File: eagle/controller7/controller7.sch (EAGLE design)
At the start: 67 parts, among them Q1 MOSFET-NCHANNELBSS138, Q2 MOSFET-NCHANNELBSS138, Q3 MOSFET-NCHANNELBSS138, Q4 MOSFET-NCHANNELBSS138, U1 LM75AIM, U2 MP2307, U3 MP2307, X2 ZX62D-B-5PA8

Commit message: controller6: minor changes
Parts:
- removed H4: MOUNT-HOLE2.8, holes:MOUNT-HOLE2.8
- removed J1: (no value), SparkFun-Connectors:M02LOCK_LONGPADS
- removed J3: (no value), SparkFun-Connectors:M05X2NO_SILK
- removed RTC1: DS3231M, SparkFun-DigitalIC:DS3231M
- removed U1: LM75AIM, NSC_By_element14_Batch_1.1:LM75AIM
- added J4: (no value), SparkFun-Connectors:M02LOCK_LONGPADS
- added J7: (no value), SparkFun-Connectors:M08X2
- added RTC2: DS3231M, SparkFun-DigitalIC:DS3231M
- added U$2: PIZERO_THROUGH_HOLE, pizero:PIZERO_THROUGH_HOLE
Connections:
- removed net N$19: U$1.2, U$1.6
- removed net VBAT: J1.1, RTC1.VBAT
- new net N$12: U$2.2, U$2.6
- new net VBAT1: J4.1, RTC2.VBAT
- net CONV_5V: no longer J3.1
- net GND: now also J4.2, RTC2.GND; no longer J1.2, J3.5, RTC1.GND, U1.GND
- net N$13: no longer J3.8
- net RX: no longer J3.7
- net SCL: now also RTC2.SCL; no longer RTC1.SCL, U1.SCL
- net SDA: now also RTC2.SDA; no longer RTC1.SDA, U1.SDA
- net TX: no longer J3.9
- net VCC: now also RTC2.VCC; no longer RTC1.VCC, U1.+VS
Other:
- moved on the sheet: JP2, VD5, VD6

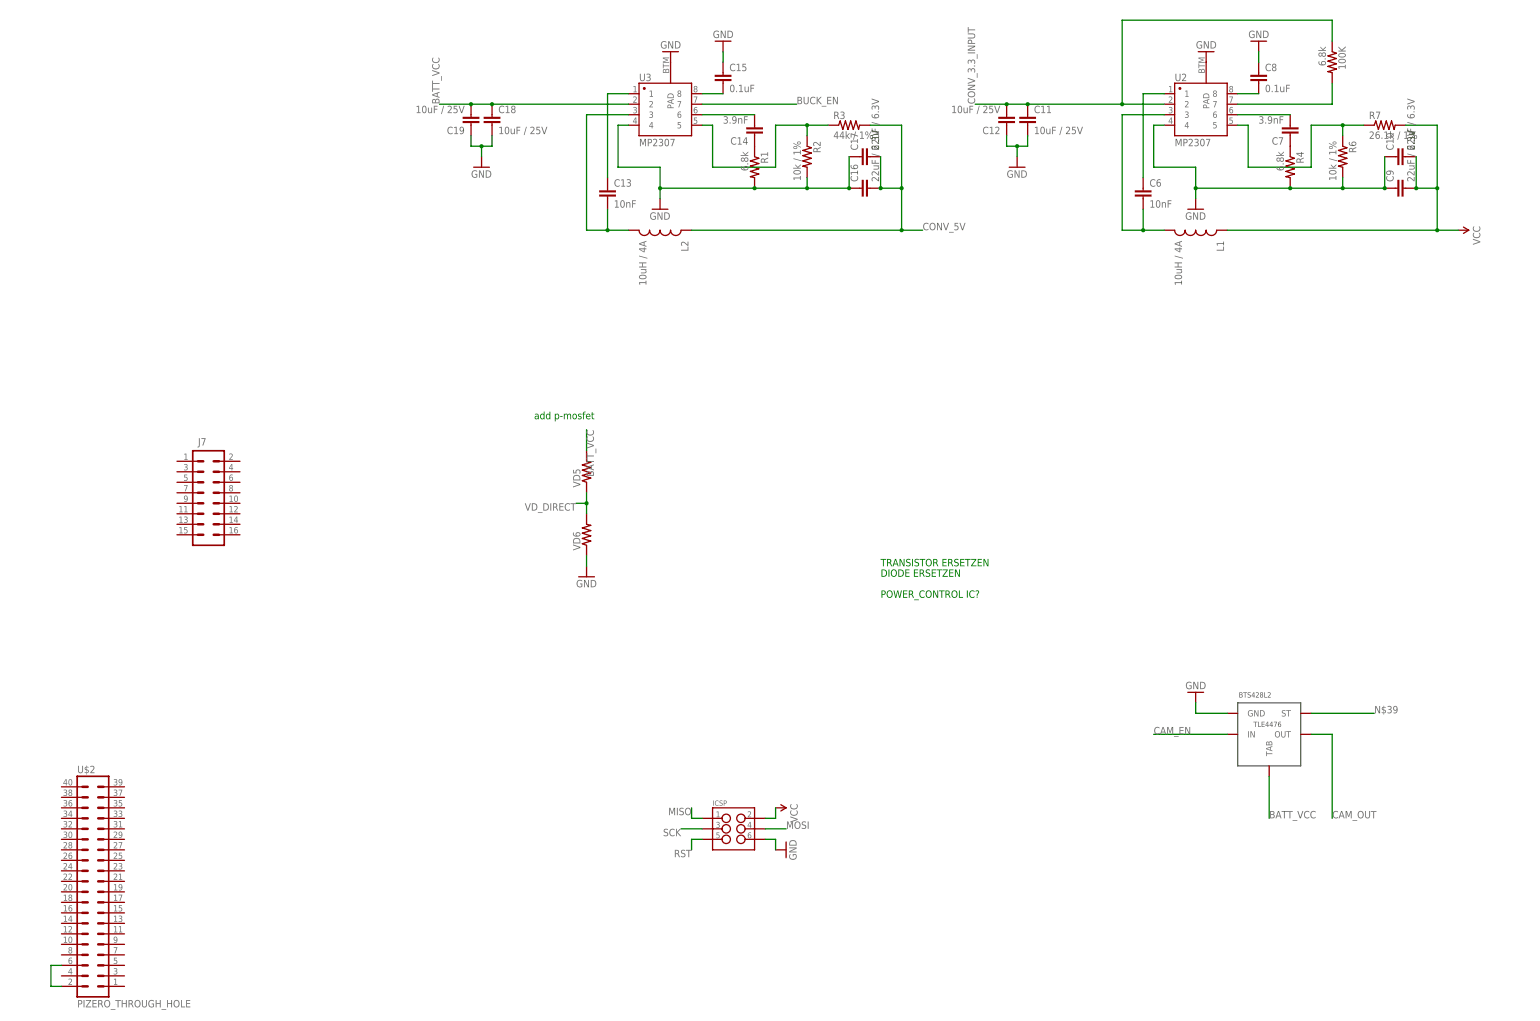
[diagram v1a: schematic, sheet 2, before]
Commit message: controller7: profet added
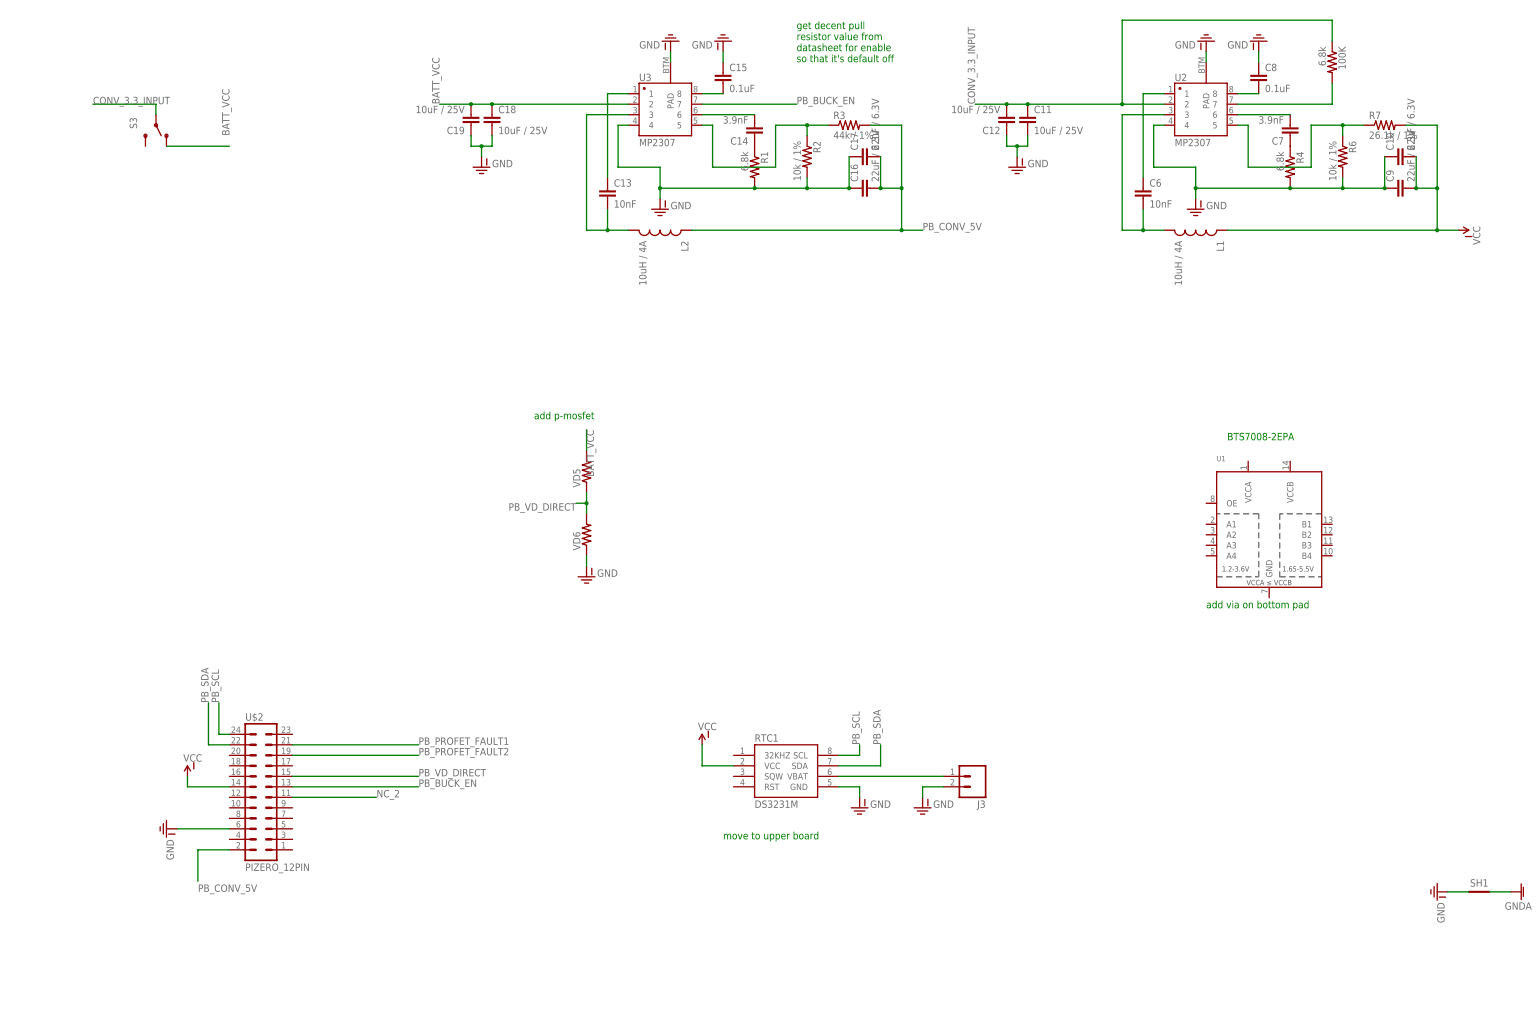
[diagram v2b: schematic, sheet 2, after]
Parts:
- removed BTS428L2: VOLTAGE_REGULATOR_TLE4476, to252:VOLTAGE_REGULATOR_TLE4476
- removed ICSP: (no value), SparkFun-Connectors:M03X2FEMALE
- removed J7: (no value), SparkFun-Connectors:M08X2
- removed JP2: JUMPER-PAD-2-NOYES_SILK, SparkFun-Passives:JUMPER-PAD-2-NOYES_SILK
- removed RTC2: DS3231M, SparkFun-DigitalIC:DS3231M
- removed S2: (no value), SparkFun-Electromechanical:SWITCH-SPDTPTH_LOCK
- removed SH: SHORT-HT5, shorts-old:SHORT-HT5
- added ICSP1: (no value), SparkFun-Connectors:M03X2FEMALE
- added J1: (no value), SparkFun-Connectors:M02LOCK
- added J3: (no value), SparkFun-Connectors:M02LOCK_LONGPADS
- added RTC1: DS3231M, SparkFun-DigitalIC:DS3231M
- added S3: (no value), SparkFun-Electromechanical:SWITCH-SPDTPTH_LOCK
- added SH1: SHORT-HT5, shorts-old:SHORT-HT5
- added U1: (no value), SparkFun-DigitalIC:TXB0104PWRSOIC14
- J4: device SparkFun-Connectors:M02LOCK_LONGPADS -> SparkFun-Connectors:M05X2PTH
- U$1, U$2: value PIZERO_THROUGH_HOLE -> PIZERO_12PIN; device pizero:PIZERO_THROUGH_HOLE -> pizero:PIZERO_12PIN
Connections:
- removed net CAM_EN: BTS428L2.IN, U$3.PC6(OC3A/!OC4A)
- removed net FOO1: U$3.PB5(OC1A/ADC12/!OC4B)
- removed net N$13: JP2.1
- removed net N$39: BTS428L2.ST
- removed net VBAT1: J4.1, RTC2.VBAT
- new net CAM_EN1: U$1.20, U$3.PB6(OC1B/OC4B/ADC13)
- new net CAM_EN2: U$1.18, U$3.PB5(OC1A/ADC12/!OC4B)
- new net CAM_OUT2: J1.2
- new net FOO: U$3.PC6(OC3A/!OC4A)
- new net GND-ISO: C10.1, C11.2, C12.1, C15.1, C16.1, C17.1, C18.2, C19.1, C8.1, C9.1, J3.2, R1.2, R2.2, R4.2, R6.2, RTC1.GND, SH1.P$1, U$2.6, U2.4, U2.PAD, U3.4, U3.PAD, VD6.1
- new net NC: U$1.11
- new net NC_2: U$2.11
- new net PB_BUCK_EN: U$2.13, U3.7
- new net PB_CONV_5V: C16.2, C17.2, L2.1, R3.2, U$2.2
- new net PB_PROFET_FAULT1: U$2.21
- new net PB_PROFET_FAULT2: U$2.19
- new net PB_SCL: RTC1.SCL, U$2.24
- new net PB_SDA: RTC1.SDA, U$2.22
- new net PB_VD_DIRECT: U$2.15, VD5.1, VD6.2
- new net PROFET_FAULT1: U$1.21, U$3.PD7(OC4D/ADC10/T0)
- new net PROFET_FAULT2: U$1.19, U$3.PD6(T1/ADC9/!OC4D)
- new net VBAT2: J3.1, RTC1.VBAT
- new net VCC-ISO: C10.2, C9.2, L1.1, R7.2, RTC1.VCC
- net BATT_VCC: now also S3.O; no longer BTS428L2.TAB, S2.O
- net BUCK_EN: now also U$1.13; no longer U3.7
- net CAM_OUT: no longer BTS428L2.OUT
- net CONV_3.3_INPUT: now also S3.P; no longer S2.P
- net CONV_5V: now also U$1.2; no longer C16.2, C17.2, L2.1, R3.2
- net FOO2: now also U$1.17; no longer U$3.PB6(OC1B/OC4B/ADC13)
- net GND: now also ICSP1.6, U$1.6; no longer BTS428L2.GND, C10.1, C11.2, C12.1, C15.1, C16.1, C17.1, C18.2, C19.1, C8.1, C9.1, ICSP.6, R1.2, R2.2, R4.2, R6.2, RTC2.GND, SH.P$1, U2.4, U2.PAD, U3.4, U3.PAD, VD6.1
- net GNDA: now also J1.1, SH1.P$2; no longer SH.P$2
- net MISO: now also ICSP1.1; no longer ICSP.1
- net MOSI: now also ICSP1.4; no longer ICSP.4
- net N$12: now also U$1.16; no longer U$2.2, U$2.6
- net N$22: no longer S2.S
- net RST: now also ICSP1.5; no longer ICSP.5, JP2.2
- net RX: now also U$1.8
- net SCK: now also ICSP1.3; no longer ICSP.3
- net SCL: now also J4.10; no longer RTC2.SCL
- net SDA: now also J4.8; no longer RTC2.SDA
- net TX: now also U$1.10
- net VCC: now also ICSP1.2, J4.4, U$1.14; no longer C10.2, C9.2, ICSP.2, L1.1, R7.2, RTC2.VCC
- net VD_DIRECT: now also U$1.15; no longer VD5.1, VD6.2
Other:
- note added: "BTS7008-2EPA"
- note added: "add via on bottom pad"
- note added: "get decent pull resistor value from datasheet for enable so that it's default off"
- note added: "move to upper board"
- note removed: "3.3V"
- note removed: "5V"
- note removed: "DIODE ERSETZEN"
- note removed: "POWER_CONTROL IC?"
- note removed: "STEP-DOWN-CONVERTER"
- note removed: "Short between Power-GND and Signal-GND"
- note removed: "TRANSISTOR ERSETZEN"
- moved on the sheet: J6, J8, R9

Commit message: controller7: routing power board created display board
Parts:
- removed J6, J8: (no value), SparkFun-Connectors:M02LOCK
- removed Q3, Q4: MOSFET-NCHANNELBSS138, SparkFun-DiscreteSemi:MOSFET-NCHANNELBSS138
- removed RTC1: DS3231M, SparkFun-DigitalIC:DS3231M
- removed U1: (no value), SparkFun-DigitalIC:TXB0104PWRSOIC14
- added IC1, IC2: ILD213T, SparkFun-DiscreteSemi:ILD213T
- added J10, J7, J9: (no value), SparkFun-Connectors:M02LOCK
- added JP1: JUMPER-PAD-2-NOYES_SILK, SparkFun-Passives:JUMPER-PAD-2-NOYES_SILK
- added R15, R18, R19, R20: (no value), SparkFun-Passives:RESISTOR0805-RES
- added R16, R17, R21, R22, R30: (no value), SparkFun-Passives:RESISTOR1206
- added RTC2: DS3231M, SparkFun-DigitalIC:DS3231M
- added RV1: (no value), SparkFun-Electromechanical:POT
- added S2, S4, S5, S6: (no value), SparkFun-Retired:TAC_SWITCHPTH
- added U$7: BTS7008-2EPA, SparkFun-DigitalIC:BTS7008-2EPA
- added U$8: PIZERO_12PIN, pizero:PIZERO_12PIN
- added X1: 1501_04, con-lumberg:1501_04
- C3: device SparkFun-Passives:CAP0805 -> SparkFun-Passives:CAP1206
- J1: device SparkFun-Connectors:M02LOCK -> SparkFun-Connectors:M04LOCK
- J3: device SparkFun-Connectors:M02LOCK_LONGPADS -> SparkFun-Connectors:M04LOCK
- J4: device SparkFun-Connectors:M05X2PTH -> SparkFun-Connectors:M02PTH
- L1, L2: device SparkFun-Passives:INDUCTORSDR0403-560KL -> SparkFun-Passives:INDUCTORSRU1038
- Q1: value MOSFET-NCHANNELBSS138 -> 2.5A/30V; device SparkFun-DiscreteSemi:MOSFET-NCHANNELBSS138 -> SparkFun-DiscreteSemi:MOSFET-PCHANNELDMG2307L
- Q2: value MOSFET-NCHANNELBSS138 -> 200mA/50V
- R11, R12, R13, R14, RUSB1, RUSB2: device SparkFun-Passives:RESISTOR0805-RES -> SparkFun-Passives:RESISTOR1206
- U$2: value PIZERO_12PIN -> PIZERO_10PIN; device pizero:PIZERO_12PIN -> pizero:PIZERO_10PIN
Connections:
- removed net CAM_OUT: J8.2
- removed net CONV_3.3_INPUT: 100K.1, C11.1, C12.2, S3.P, U2.2
- removed net FOO: U$3.PC6(OC3A/!OC4A)
- removed net FOO2: U$1.17
- removed net PB_PROFET_FAULT1: U$2.21
- removed net PB_PROFET_FAULT2: U$2.19
- removed net PB_SCL: RTC1.SCL, U$2.24
- removed net PB_SDA: RTC1.SDA, U$2.22
- removed net PROFET_FAULT1: U$1.21, U$3.PD7(OC4D/ADC10/T0)
- removed net PROFET_FAULT2: U$1.19, U$3.PD6(T1/ADC9/!OC4D)
- removed net VBAT2: J3.1, RTC1.VBAT
- new net 3.3V: J1.2, J3.1, RV1.A, S2.4, S4.4, S5.4, S6.4, U$8.6
- new net ANALOG_IO: U$1.24, U$3.PB6(OC1B/OC4B/ADC13)
- new net BATT_VCC_RAW: J7.2, S3.O
- new net CAM_OUT1: J9.2, U$7.OUT0
- new net DB_ANALOG_IO: RV1.S, U$8.24
- new net DB_BTN: S6.2, U$8.22
- new net DB_SCL: J1.3, J3.3, U$8.21
- new net DB_SDA: J1.4, J3.4, U$8.23
- new net FOO15: U$3.PB7(OC0A/OC1C/RTS)
- new net FOO8: U$3.PB0(SS)
- new net FOOA: U$3.PB4(ADC11)
- new net N$13: IC2.A2, R19.2
- new net N$15: IC1.A2, R15.2
- new net N$19: IC1.A1, R20.2
- new net N$34: IC1.ET1, IC1.ET2, IC2.ET1, IC2.ET2, J2.7, JP1.2, X1.1
- new net N$35: J2.8, Q1.D
- new net N$36: Q1.G, Q2.S, R10.1
- new net N$37: J1.1
- new net N$38: R14.1, S5.2
- new net N$39: R30.2, S4.2
- new net N$40: R21.2, S2.2
- new net N$43: R22.2, RV1.E
- new net PB_CAM_EN1: R11.1, U$2.20, U$7.IN0
- new net PB_CAM_EN2: R12.2, U$2.15, U$7.IN1
- new net PB_PROFET_1: R17.1, U$2.18, U$7.DEN
- new net PB_PROFET_2: U$2.19, U$7.IS
- new net PB_PROFET_3: R16.2, U$2.17, U$7.DSEL
- new net PROFET1: U$1.18, U$3.PF6(ADC6/TDO)
- new net PROFET2: U$1.19, U$3.PF5(ADC5/TMS)
- new net PROFET3: U$1.17, U$3.PF4(ADC4/TCK)
- new net SWITCH_USB_VCC: Q2.G, U$3.PD5(XCK/CTS)
- new net VBAT1: J4.1, RTC2.VBAT
- new net VCC_2: R14.2, R21.1, R22.1, R30.1, U$8.14
- net BATT_VCC: now also 100K.1, C11.1, C12.2, S3.P, U$7.VS, U2.2; no longer J6.2, S3.O
- net BTN: now also U$1.22, U$3.PC7(ICP3/CLK0/OC4A); no longer U$3.PF7(ADC7(TDI)
- net BUCK_EN: now also U$1.16, U$3.PE6(INT.6/AIN0); no longer U$1.13, U$3.PB7(OC0A/OC1C/RTS)
- net CAM1: now also R20.1, U$3.PB5(OC1A/ADC12/!OC4B); no longer Q1.G, R10.2, U$3.PF1(ADC1)
- net CAM2: now also R15.1, U$3.PD7(OC4D/ADC10/T0); no longer Q2.G, R11.2, U$3.PF4(ADC4/TCK)
- net CAM3: now also R18.1, U$3.PD6(T1/ADC9/!OC4D); no longer Q3.G, R12.2, U$3.PF5(ADC5/TMS)
- net CAM4: now also R19.1, U$3.PD4(ICP1/ADC8); no longer Q4.G, R13.1, U$3.PF6(ADC6/TDO)
- net CAM_EN1: now also U$3.PF7(ADC7(TDI); no longer U$3.PB6(OC1B/OC4B/ADC13)
- net CAM_EN2: now also U$1.15, U$3.PF1(ADC1); no longer U$1.18, U$3.PB5(OC1A/ADC12/!OC4B)
- net CAM_OUT2: now also J10.2, U$7.OUT1; no longer J1.2
- net CONV_5V: now also Q1.S, R10.2
- net GND: now also IC1.C1, IC1.C2, IC2.C1, IC2.C2, JP1.1, Q2.D, RTC2.GND; no longer J2.7, Q1.S, Q2.S, Q3.S, R14.1
- net GND-ISO: now also R11.2, R12.1, R16.1, R17.2, U$7.GND; no longer J3.2, RTC1.GND
- net GNDA: now also J10.1, J7.1, J9.1; no longer J1.1, J6.1, J8.1
- net LED: now also U$3.PC6(OC3A/!OC4A); no longer U$3.PC7(ICP3/CLK0/OC4A)
- net N$12: now also IC2.A1, R18.2; no longer U$1.16
- net N$16: no longer Q4.D
- net N$18: now also IC1.CT2, R13.1; no longer Q4.S, R14.2
- net N$31: now also IC1.CT1, X1.3; no longer Q1.D, R10.1
- net N$32: now also IC2.CT2, X1.2; no longer Q2.D, R11.1
- net N$33: now also IC2.CT1; no longer Q3.D, R12.1
- net PB_BUCK_EN: now also U$2.16; no longer U$2.13
- net PB_VD_DIRECT: now also U$2.13; no longer U$2.15
- net SCL: now also RTC2.SCL, U$1.21; no longer J4.10
- net SDA: now also RTC2.SDA, U$1.23; no longer J4.8
- net VCC: now also RTC2.VCC; no longer J4.4
- net VCC-ISO: now also U$2.14; no longer RTC1.VCC
- net VD_DIRECT: now also U$1.13; no longer U$1.15
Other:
- note added: "check if we really want to include the resistor"
- note added: "is it possible to make this lumix compatible?"
- note added: "mosfet"
- note added: "power lines via SPI headers"
- note added: "some lines ought to be power lines (width)"
- note removed: "(optional) Resistor may cause trouble"
- note removed: "add p-mosfet"
- note removed: "is this resistor really right?"
- note removed: "move to upper board"
- moved on the sheet: J2, J5, Q1, Q2, R10, R13, S3, SH1, U2, U3

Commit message: controller7: power board finished
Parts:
- added J6: (no value), SparkFun-Connectors:M03X2FEMALE
- added R24: 100K, SparkFun-Resistors:RESISTOR0805-RES
- R23: value 6.8k -> 100K
- RRST: device SparkFun-Passives:RESISTOR0805-RES -> SparkFun-Passives:RESISTOR1206
- S1: device SparkFun-Retired:TAC_SWITCHSMD -> SparkFun-Retired:TAC_SWITCHPTH
- renumbered 100K to R23, VD5 to VD1, VD6 to VD2
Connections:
- removed net N$38: R14.1, S5.2
- removed net N$39: R30.2, S4.2
- removed net N$40: R21.2, S2.2
- new net DB_MISO: J6.1, R21.2, S2.2
- new net DB_MOSI: J6.4, R14.1, S5.2
- new net DB_RST: J6.5
- new net DB_SCK: J6.3, R30.2, S4.2
- new net N$45: J6.2
- new net N$46: J6.6
- net BATT_VCC: now also R24.1
- net CAM_EN1: now also U$3.PF6(ADC6/TDO); no longer U$3.PF7(ADC7(TDI)
- net PB_BUCK_EN: now also R24.2
- net PROFET1: now also U$3.PF4(ADC4/TCK); no longer U$3.PF6(ADC6/TDO)
- net PROFET2: now also U$3.PF7(ADC7(TDI); no longer U$3.PF5(ADC5/TMS)
- net PROFET3: now also U$3.PF5(ADC5/TMS); no longer U$3.PF4(ADC4/TCK)
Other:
- note added: "I2C temp sensor?"
- note added: "Molex KK 254 RPC"
- note removed: "add via on bottom pad"
- note removed: "get decent pull resistor value from datasheet for enable so that it's default off"
- note removed: "some lines ought to be power lines (width)"
